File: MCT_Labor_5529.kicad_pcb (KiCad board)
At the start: 2 copper layers, 160 x 100 mm, 155 parts, among them J1 Micro_SD_Card_Det, J10 Conn_01x04_Male, J11 Conn_01x01_Female, J12 Conn_01x01_Female, J13 Conn_01x01_Female, J14 Conn_02x05_Odd_Even, J15 Conn_01x02, J18 Screw_Terminal_01x02, J2 Conn_02x05_Odd_Even, J3 Grove, J4 Conn_02x04_Odd_Even, J5 Grove, J6 Grove, J7 Conn_01x04_Male, J8 Conn_01x01_Female, J9 Conn_01x01_Female, Q1 BSS138, SW1 SW_Push, SW2 SW_Push, SW3 SW_SPDT, U1 RC1602A, U10 msp-exp430f5529-LP, U11 MCP73831, U12 TPS73733, U13 TLV61048, U14 LM2776, U2 ULN2003, U3 74148, U4 74_138, U5 NRF24L01_Breakout, U6 74HCT595, U7 ESP-12E, U8 TMP411, U9 STC3100, X1 XBee_S3

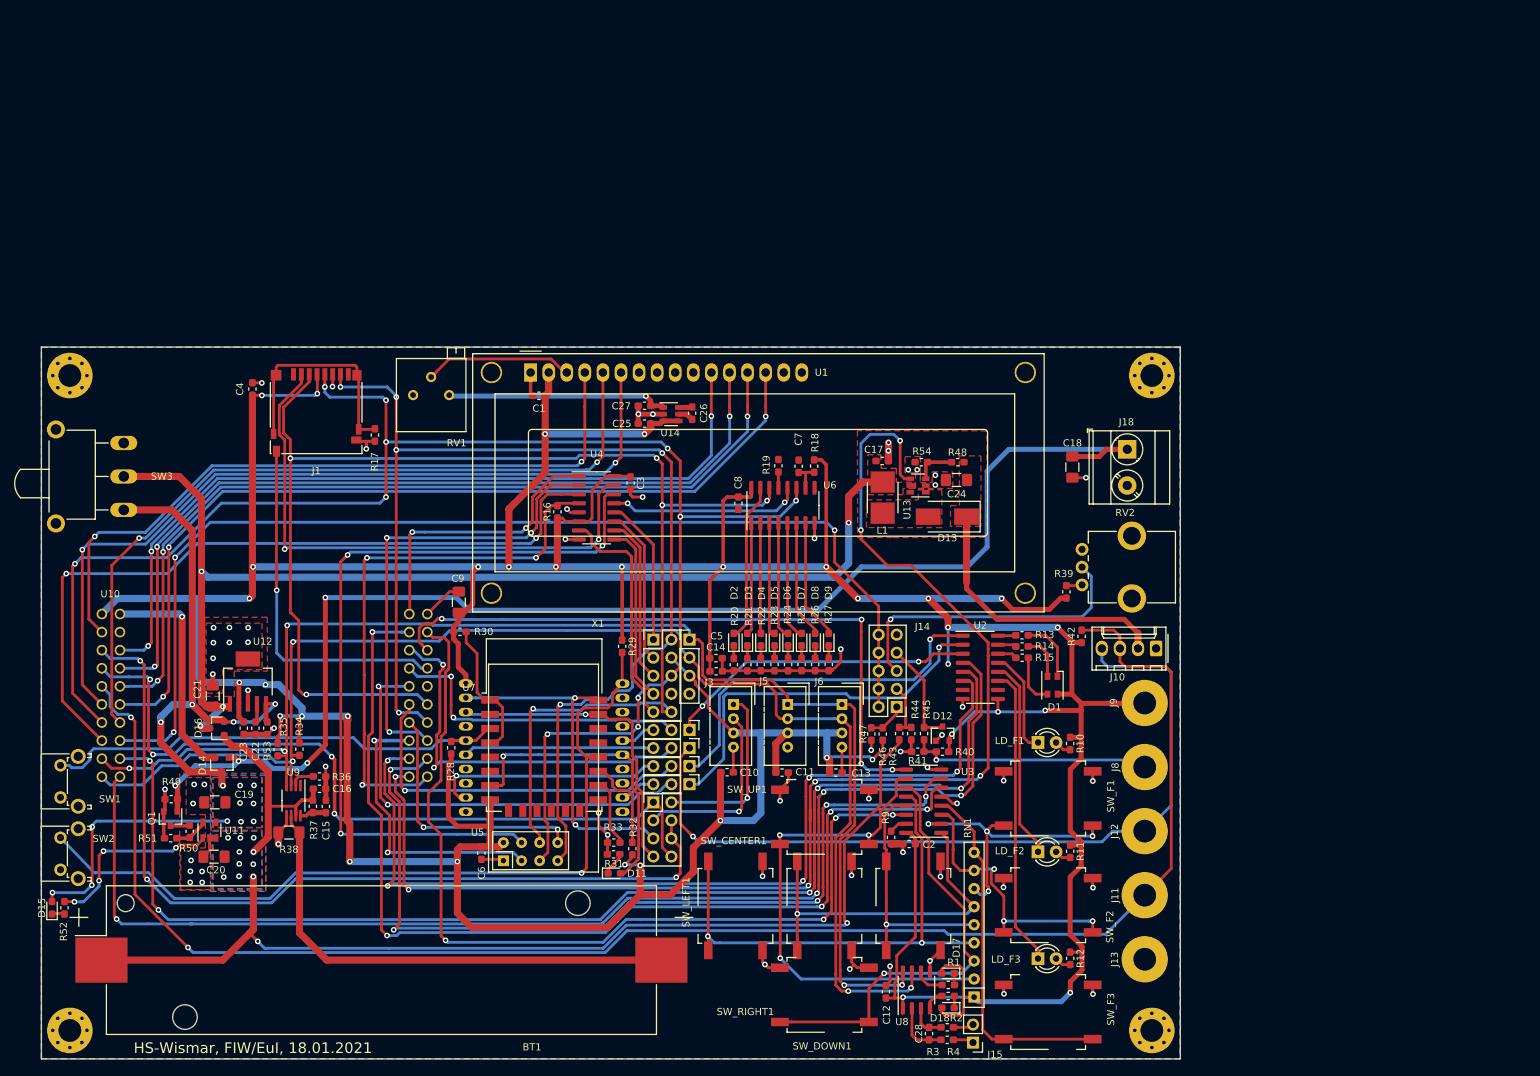
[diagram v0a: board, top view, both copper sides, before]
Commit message: Open Hardware Logo eingefügt
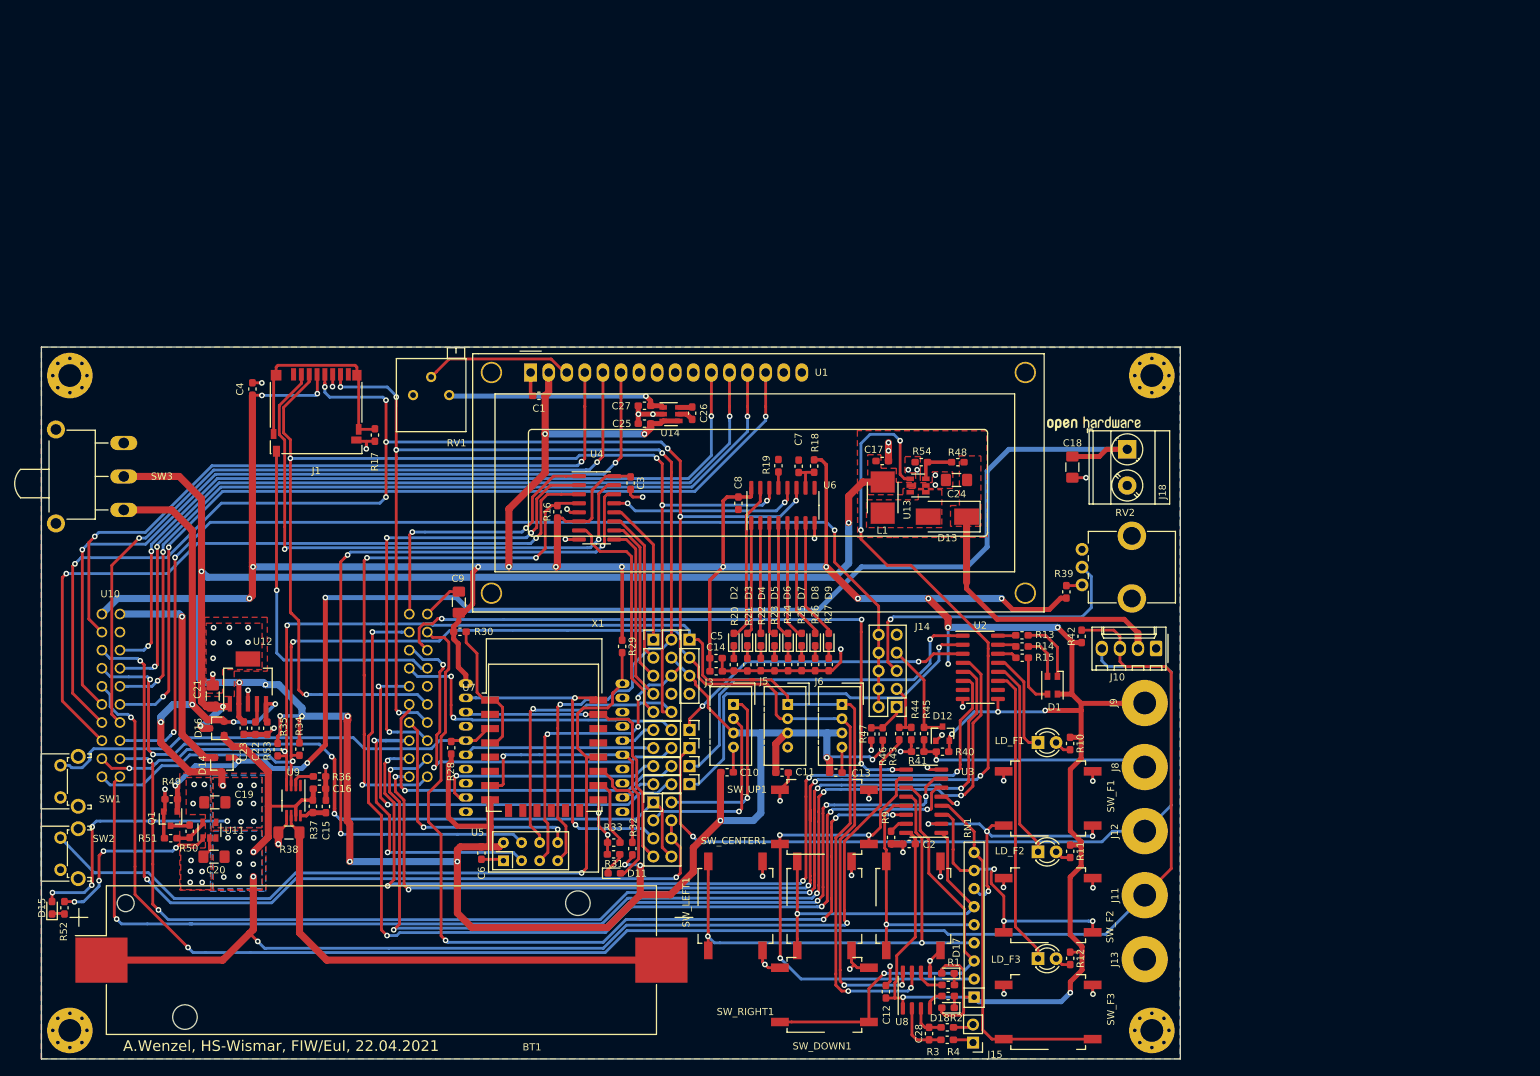
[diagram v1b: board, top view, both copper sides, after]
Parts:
- removed G***: LOGO, HS-Wismar:hs-logo_8mm
- added REF**: OSHW-Logo2_14.6x12mm_SilkScreen, HS-Wismar:OSHW-Logo2_14.6x12mm_SilkScreen, F.Cu at (197.8, 56.2)
- R13: value 120 -> 220
- R14, R15: value 39 -> 47
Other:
- board text added: "A.Wenzel, HS-Wismar, FIW/EuI, 22.04.2021"
- board text removed: "HS-Wismar, FIW/EuI, 18.01.2021"

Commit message: Vorbereitet für Release für Group-Buy
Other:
- rule pad_to_mask_clearance: 0.05 -> 0

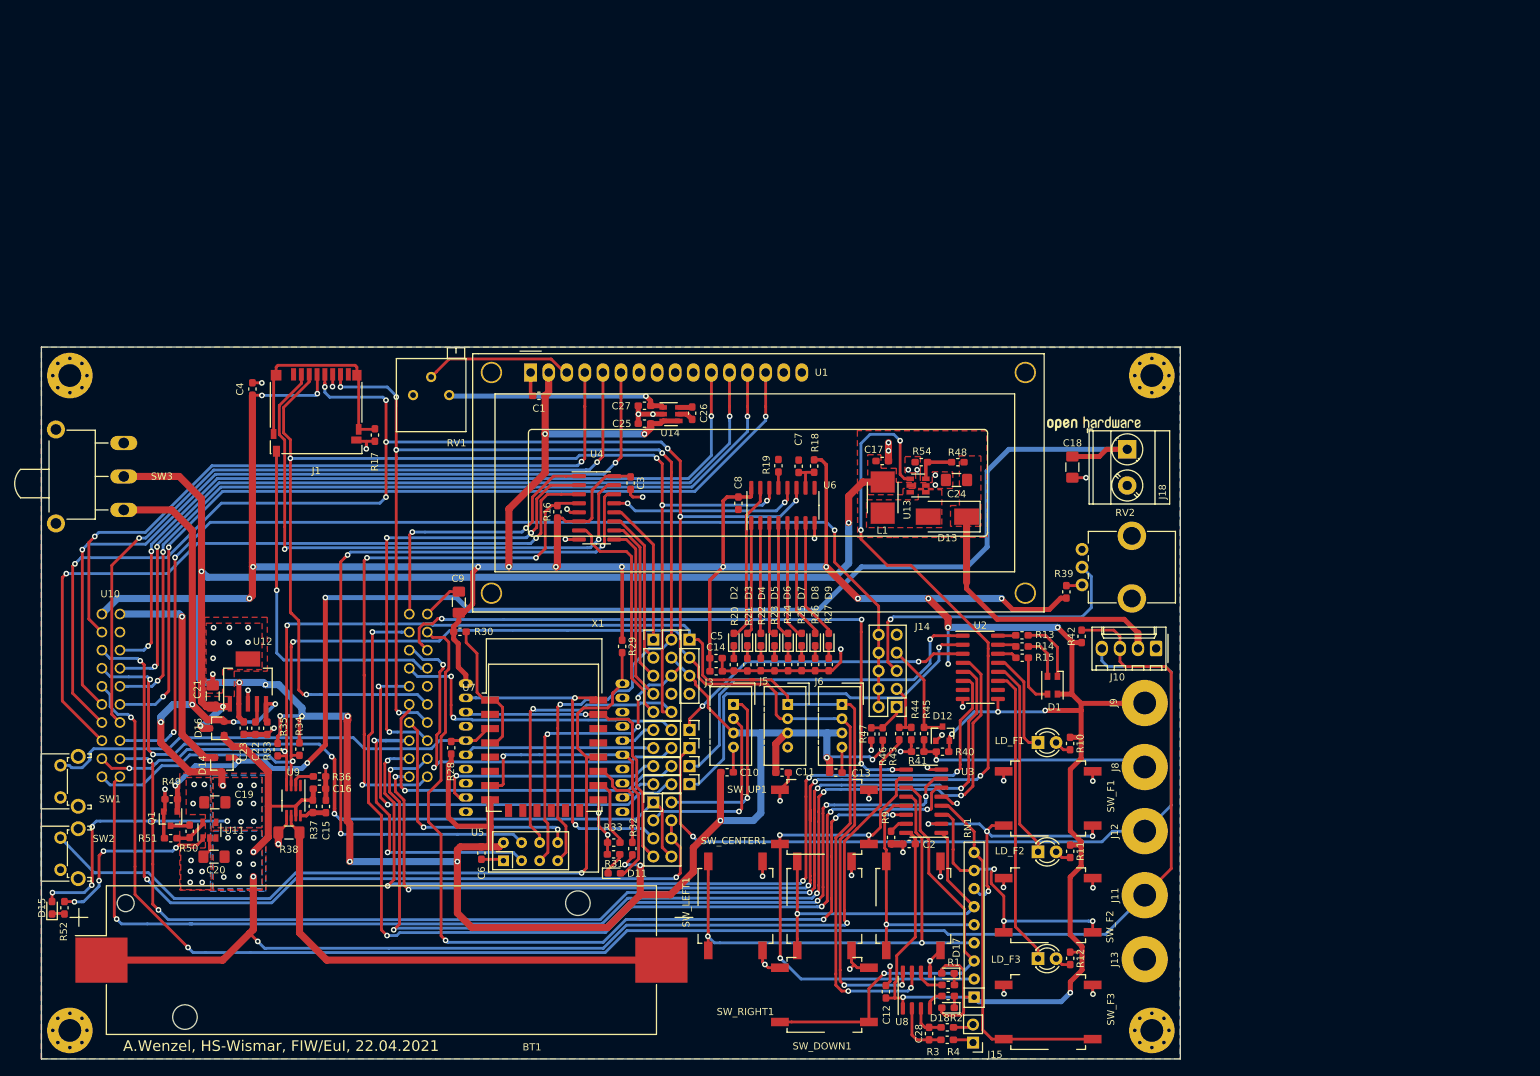
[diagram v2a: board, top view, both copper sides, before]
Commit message: Switched ESP8266F to MICRO32
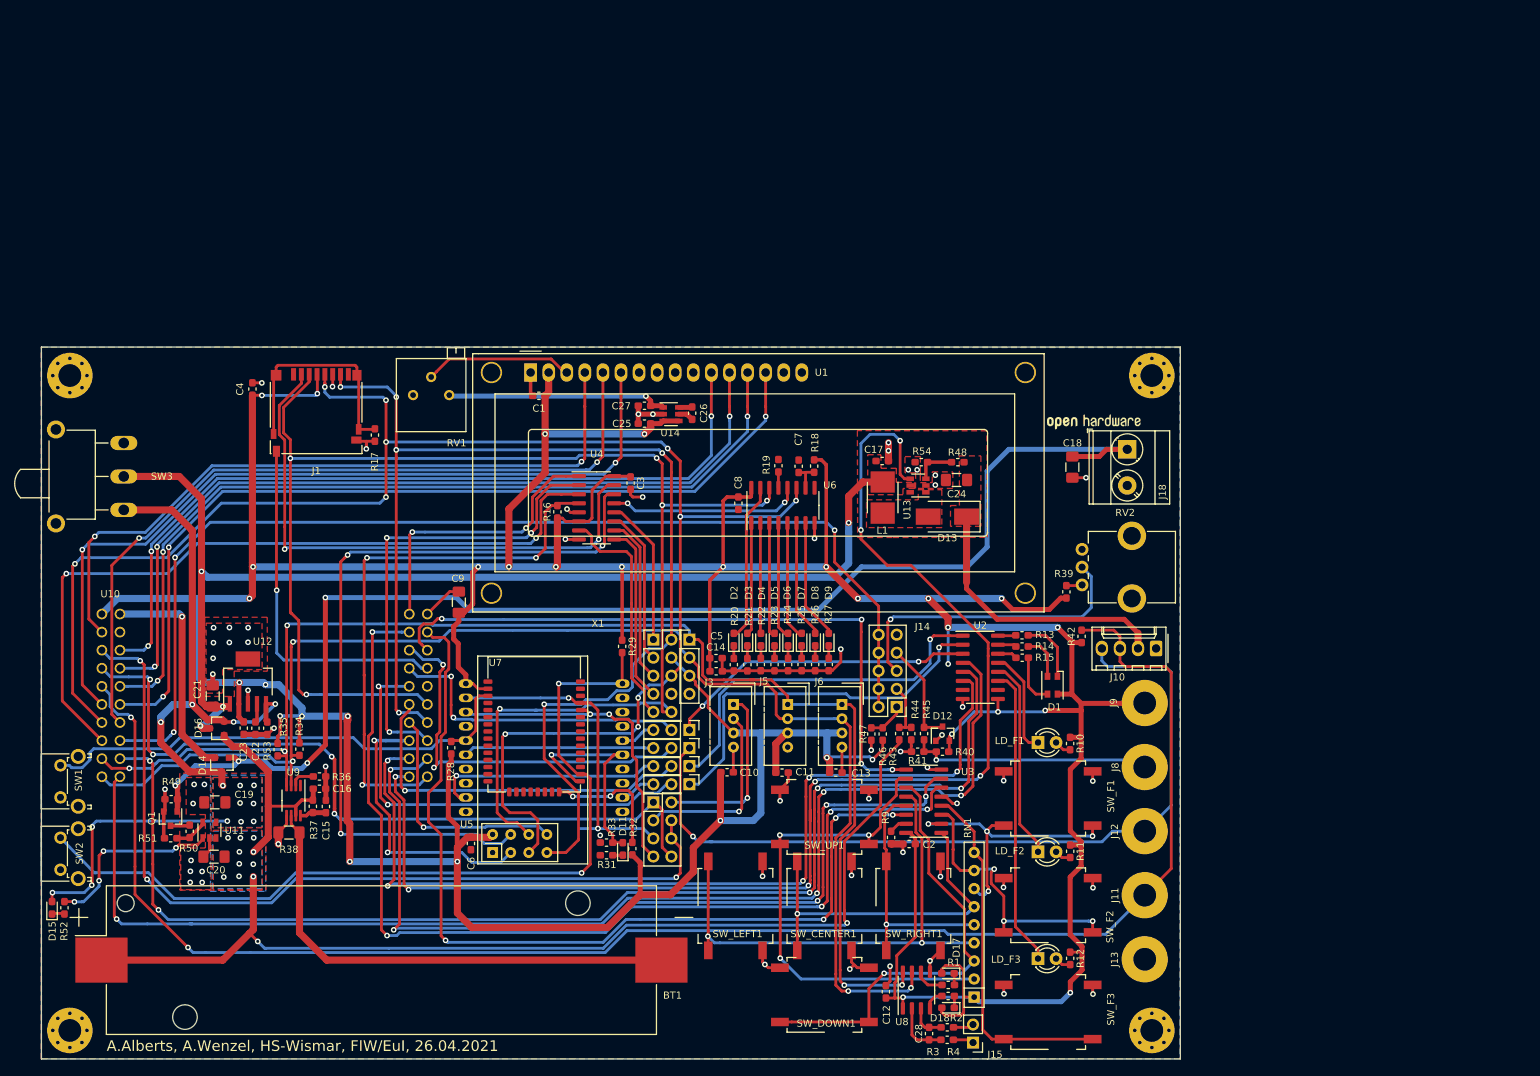
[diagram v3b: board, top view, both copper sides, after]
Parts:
- removed R30: 10k, Resistor_SMD:R_0603_1608Metric_Pad1.05x0.95mm_HandSolder
- U7: value ESP-12E -> Micro-32; footprint RF_Module:ESP-12E -> HS-Wismar:micro32
- moved U7 9.50 mm to (119.2, 112.5)
- moved D11 3.63 mm to (131.7, 120.5), turned to 90 degrees
- moved C6 2.00 mm to (110.3, 119.7)
- moved U5 1.91 mm to (113.4, 121.0)
- moved R33 1.02 mm to (129.4, 119.6)
- moved R31 1.00 mm to (129.4, 121.4)
- moved REF** 0.25 mm to (197.8, 56.0)
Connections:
- R33 pad 1: Net-(R33-Pad1) -> Net-(D11-Pad2)
- U7 pad 1: Net-(R30-Pad2) -> GND
- U7 pad 16: Net-(R33-Pad1) -> Net-(U7-Pad16)
- U7 pad 17: Net-(R32-Pad2) -> Net-(U7-Pad17)
- U7 pad 18: Net-(R29-Pad2) -> Net-(U7-Pad18)
- U7 pad 2: Net-(U7-Pad2) -> +3V3
- U7 pad 21: Net-(J4-Pad7) -> Net-(U7-Pad21)
- U7 pad 22: Net-(J4-Pad5) -> Net-(U7-Pad22)
- U7 pad 4: Net-(R30-Pad2) -> Net-(U7-Pad4)
- U7 pad 7: Net-(D11-Pad2) -> Net-(U7-Pad7)
- U7 pad 8: +3V3 -> Net-(U7-Pad8)
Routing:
- net Net-(R30-Pad2): track 19.8 -> 0.00 mm
- net GND: track 152.8 -> 141.4 mm, vias 62 -> 61
- net Net-(R33-Pad1): track 9.71 -> 0.00 mm
- net Net-(D11-Pad2): track 41.9 -> 32.6 mm
- net /Launchpad/P3.2: track 231.3 -> 239.9 mm
- net +3V3: track 775.3 -> 767.8 mm, vias 35 -> 33
- net /SPI/MOSI: track 211.9 -> 217.7 mm
- net /SPI/MISO: track 167.9 -> 173.4 mm
- net Net-(R29-Pad2): track 116.6 -> 121.5 mm, vias 1 -> 2
- net Net-(R32-Pad2): track 13.4 -> 18.3 mm, vias 0 -> 2
- net Net-(R28-Pad2): track 66.8 -> 71.0 mm
- net /SPI/NRF_INT: track 36.4 -> 33.4 mm, vias 2 -> 1
- net Net-(J4-Pad5): track 49.4 -> 47.1 mm
- net Net-(D11-Pad1): track 3.35 -> 1.42 mm
- net Net-(J4-Pad7): track 44.0 -> 45.6 mm, vias 1 -> 2
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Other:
- board text added: "A.Alberts, A.Wenzel, HS-Wismar, FIW/EuI, 26.04.2021"
- board text removed: "A.Wenzel, HS-Wismar, FIW/EuI, 22.04.2021"

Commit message: Alternative Footprints für Taster und LCD eingefügt
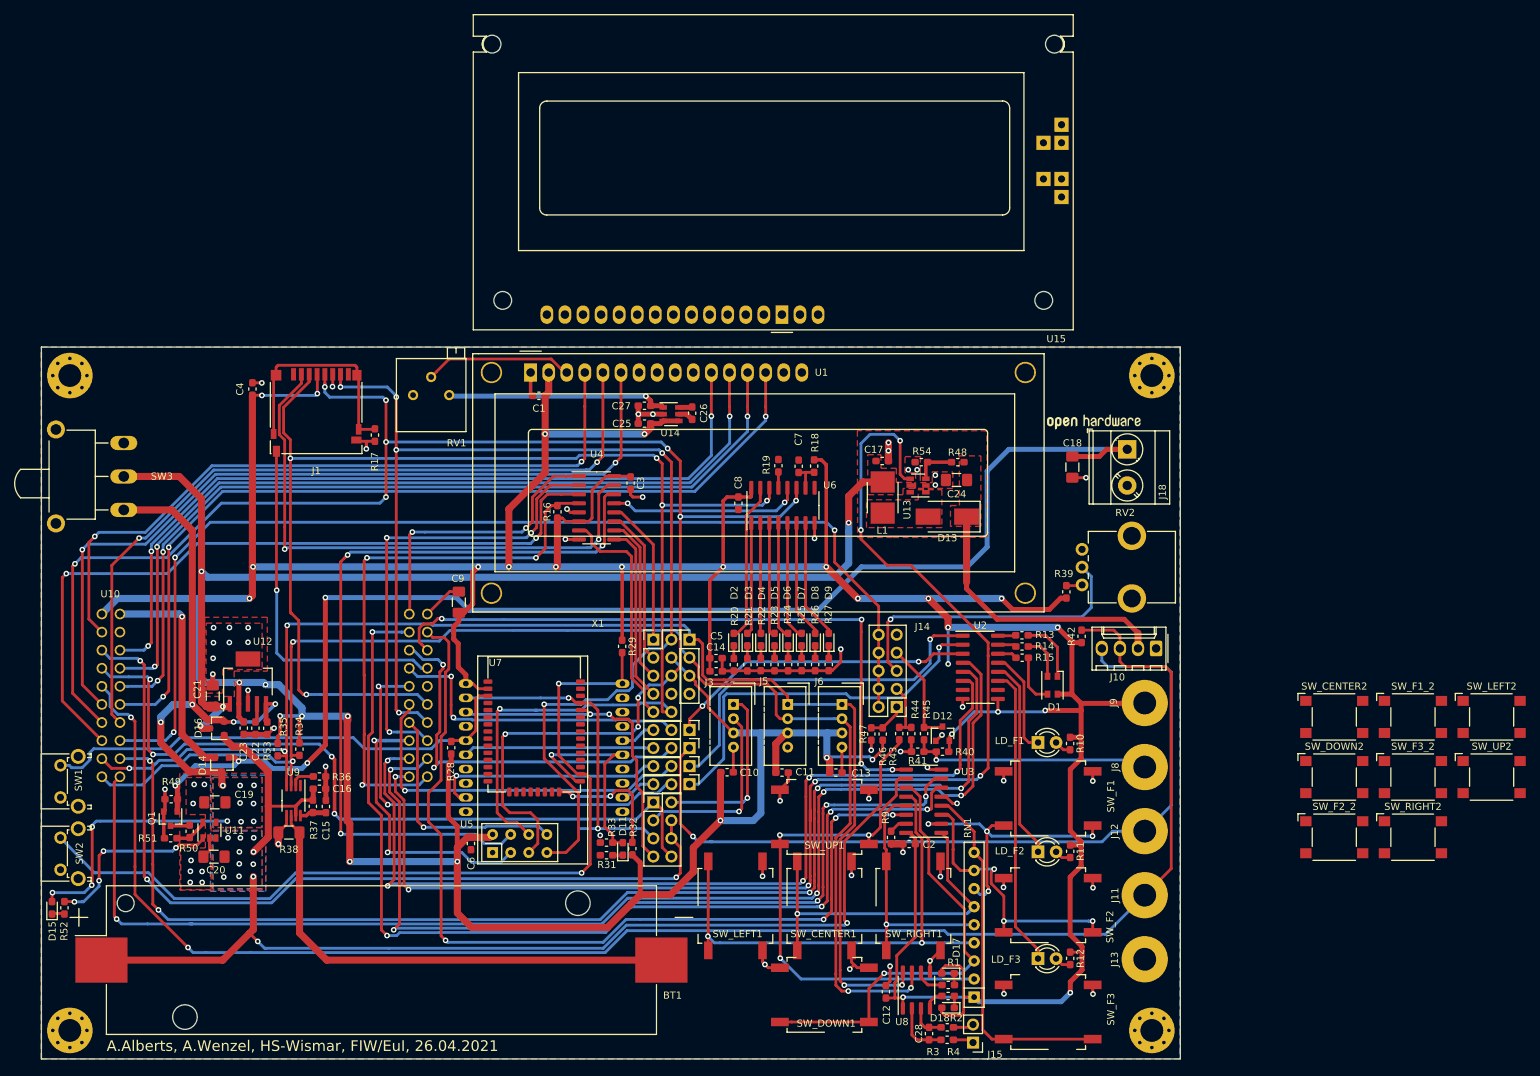
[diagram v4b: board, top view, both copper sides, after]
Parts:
- added SW_CENTER2: SW_MEC_5G, Button_Switch_SMD:SW_SPST_Omron_B3FS-100xP, F.Cu at (231.6, 102.0)
- added SW_DOWN2: SW_MEC_5G, Button_Switch_SMD:SW_SPST_Omron_B3FS-100xP, F.Cu at (231.6, 110.4)
- added SW_F1_2: SW_MEC_5, Button_Switch_SMD:SW_SPST_Omron_B3FS-100xP, F.Cu at (242.7, 102.0)
- added SW_F2_2: SW_MEC_5G, Button_Switch_SMD:SW_SPST_Omron_B3FS-100xP, F.Cu at (231.6, 118.9)
- added SW_F3_2: SW_MEC_5G, Button_Switch_SMD:SW_SPST_Omron_B3FS-100xP, F.Cu at (242.7, 110.4)
- added SW_LEFT2: SW_MEC_5G, Button_Switch_SMD:SW_SPST_Omron_B3FS-100xP, F.Cu at (253.7, 102.0)
- added SW_RIGHT2: SW_MEC_5G, Button_Switch_SMD:SW_SPST_Omron_B3FS-100xP, F.Cu at (242.7, 118.9)
- added SW_UP2: SW_MEC_5G, Button_Switch_SMD:SW_SPST_Omron_B3FS-100xP, F.Cu at (253.7, 110.4)
- added U15: RC1602A, Display:RC1602A, F.Cu at (154.0, 45.4)
